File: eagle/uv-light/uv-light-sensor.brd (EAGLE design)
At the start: 17 x 13 mm, 4 parts, among them IC100 SI1147

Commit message: CHG: updated lib, schematics and boards
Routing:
- net GND: vias 0 -> 53
- added copper zone on layer 16, net GND
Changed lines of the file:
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@@
 <element name="IC100" library="weather_station" package="QFN-10/2MM" value="SI1147" x="12.065" y="8.89" smashed="yes" rot="R90">
 <attribute name="DIGIKEY" value="336-2624-1-ND" x="26.035" y="24.13" size="1.778" layer="27" rot="R90" display="off"/>
-<attribute name="NAME" x="14.31625" y="8.89" size="1.016" layer="25" font="vector" ratio="12" rot="R90" align="bottom-center"/>
+<attribute name="NAME" x="11.1125" y="11.45875" size="1.016" layer="25" font="vector" ratio="12" rot="R180" align="center"/>
 </element>
 <element name="C100" library="rcl" package="C0603" value="100n" x="8.255" y="8.5725" smashed="yes">
-<attribute name="NAME" x="7.14375" y="10.00125" size="1.27" layer="25"/>
+<attribute name="NAME" x="8.255" y="10.31875" size="1.016" layer="25" align="center"/>
 <attribute name="VALUE" x="7.62" y="6.6675" size="1.27" layer="27"/>
 </element>
 <element name="LINK" library="pinhead" package="1X06" value="" x="8.255" y="5.23875" smashed="yes">
-<attribute name="NAME" x="11.3538" y="2.30505" size="1.27" layer="25" ratio="10"/>
+<attribute name="NAME" x="8.1788" y="2.7813" size="1.016" layer="25" ratio="10" align="center"/>
 <attribute name="VALUE" x="0.635" y="2.06375" size="1.27" layer="27"/>
 </element>
 <element name="SOLAR" library="pinhead" package="1X02" value="" x="3.175" y="8.5725" smashed="yes" rot="R180">
-<attribute name="NAME" x="6.7437" y="11.5062" size="1.27" layer="25" ratio="10" rot="R180"/>
+<attribute name="NAME" x="3.2512" y="10.8712" size="1.016" layer="25" ratio="10" rot="R180" align="center"/>
 <attribute name="VALUE" x="5.715" y="11.7475" size="1.27" layer="27" rot="R180"/>
 </element>
@@
 <wire x1="11.7475" y1="10.4775" x2="11.815" y2="10.41" width="0.254" layer="1"/>
 <wire x1="11.815" y1="10.41" x2="11.815" y2="9.84" width="0.254" layer="1"/>
-<polygon width="0.4064" layer="1" thermals="no">
+<polygon width="0.3048" layer="1" thermals="no">
 <vertex x="0" y="13"/>
 <vertex x="0" y="0"/>
@@
 <vertex x="17" y="13"/>
 </polygon>
+<via x="3.81" y="0.635" extent="1-16" drill="0.3"/>
+<polygon width="0.3048" layer="16" thermals="no">
+<vertex x="0" y="13"/>
+<vertex x="17" y="13"/>
+<vertex x="17" y="0"/>
+<vertex x="0" y="0"/>
+</polygon>
+<via x="4.7625" y="0.635" extent="1-16" drill="0.3"/>
+<via x="5.715" y="0.635" extent="1-16" drill="0.3"/>
+<via x="6.6675" y="0.635" extent="1-16" drill="0.3"/>
+<via x="7.62" y="0.635" extent="1-16" drill="0.3"/>
+<via x="8.5725" y="0.635" extent="1-16" drill="0.3"/>
+<via x="9.525" y="0.635" extent="1-16" drill="0.3"/>
+<via x="10.4775" y="0.635" extent="1-16" drill="0.3"/>
+<via x="11.43" y="0.635" extent="1-16" drill="0.3"/>
+<via x="12.3825" y="0.635" extent="1-16" drill="0.3"/>
+<via x="13.335" y="0.635" extent="1-16" drill="0.3"/>
+<via x="14.2875" y="0.635" extent="1-16" drill="0.3"/>
+<via x="15.24" y="0.635" extent="1-16" drill="0.3"/>
+<via x="16.1925" y="0.635" extent="1-16" drill="0.3"/>
+<via x="16.35125" y="1.42875" extent="1-16" drill="0.3"/>
+<via x="16.35125" y="2.38125" extent="1-16" drill="0.3"/>
+<via x="16.35125" y="3.33375" extent="1-16" drill="0.3"/>
+<via x="16.35125" y="4.28625" extent="1-16" drill="0.3"/>
+<via x="16.35125" y="5.23875" extent="1-16" drill="0.3"/>
+<via x="16.35125" y="6.19125" extent="1-16" drill="0.3"/>
+<via x="16.35125" y="7.14375" extent="1-16" drill="0.3"/>
+<via x="16.35125" y="8.09625" extent="1-16" drill="0.3"/>
+<via x="16.35125" y="9.04875" extent="1-16" drill="0.3"/>
+<via x="15.39875" y="8.73125" extent="1-16" drill="0.3"/>
+<via x="14.12875" y="9.04875" extent="1-16" drill="0.3"/>
+<via x="12.85875" y="10.95375" extent="1-16" drill="0.3"/>
+<via x="13.17625" y="11.90625" extent="1-16" drill="0.3"/>
+<via x="12.54125" y="12.3825" extent="1-16" drill="0.3"/>
+<via x="11.58875" y="12.3825" extent="1-16" drill="0.3"/>
+<via x="10.63625" y="12.3825" extent="1-16" drill="0.3"/>
+<via x="9.68375" y="12.3825" extent="1-16" drill="0.3"/>
+<via x="8.73125" y="12.3825" extent="1-16" drill="0.3"/>
+<via x="7.77875" y="12.3825" extent="1-16" drill="0.3"/>
+<via x="6.82625" y="12.3825" extent="1-16" drill="0.3"/>
+<via x="5.87375" y="12.3825" extent="1-16" drill="0.3"/>
+<via x="4.92125" y="12.3825" extent="1-16" drill="0.3"/>
+<via x="3.96875" y="12.3825" extent="1-16" drill="0.3"/>
+<via x="3.01625" y="12.3825" extent="1-16" drill="0.3"/>
+<via x="2.06375" y="12.3825" extent="1-16" drill="0.3"/>
+<via x="1.11125" y="12.3825" extent="1-16" drill="0.3"/>
+<via x="0.635" y="11.7475" extent="1-16" drill="0.3"/>
+<via x="0.635" y="10.795" extent="1-16" drill="0.3"/>
+<via x="0.635" y="9.8425" extent="1-16" drill="0.3"/>
+<via x="0.635" y="8.89" extent="1-16" drill="0.3"/>
+<via x="0.635" y="7.9375" extent="1-16" drill="0.3"/>
+<via x="0.635" y="6.985" extent="1-16" drill="0.3"/>
+<via x="0.635" y="6.0325" extent="1-16" drill="0.3"/>
+<via x="0.635" y="5.08" extent="1-16" drill="0.3"/>
+<via x="0.635" y="3.81" extent="1-16" drill="0.3"/>
+<via x="3.175" y="3.81" extent="1-16" drill="0.3"/>
+<via x="3.81" y="3.175" extent="1-16" drill="0.3"/>
+<via x="4.1275" y="2.2225" extent="1-16" drill="0.3"/>
+<via x="4.1275" y="1.42875" extent="1-16" drill="0.3"/>
 </signal>
 <signal name="N$1">

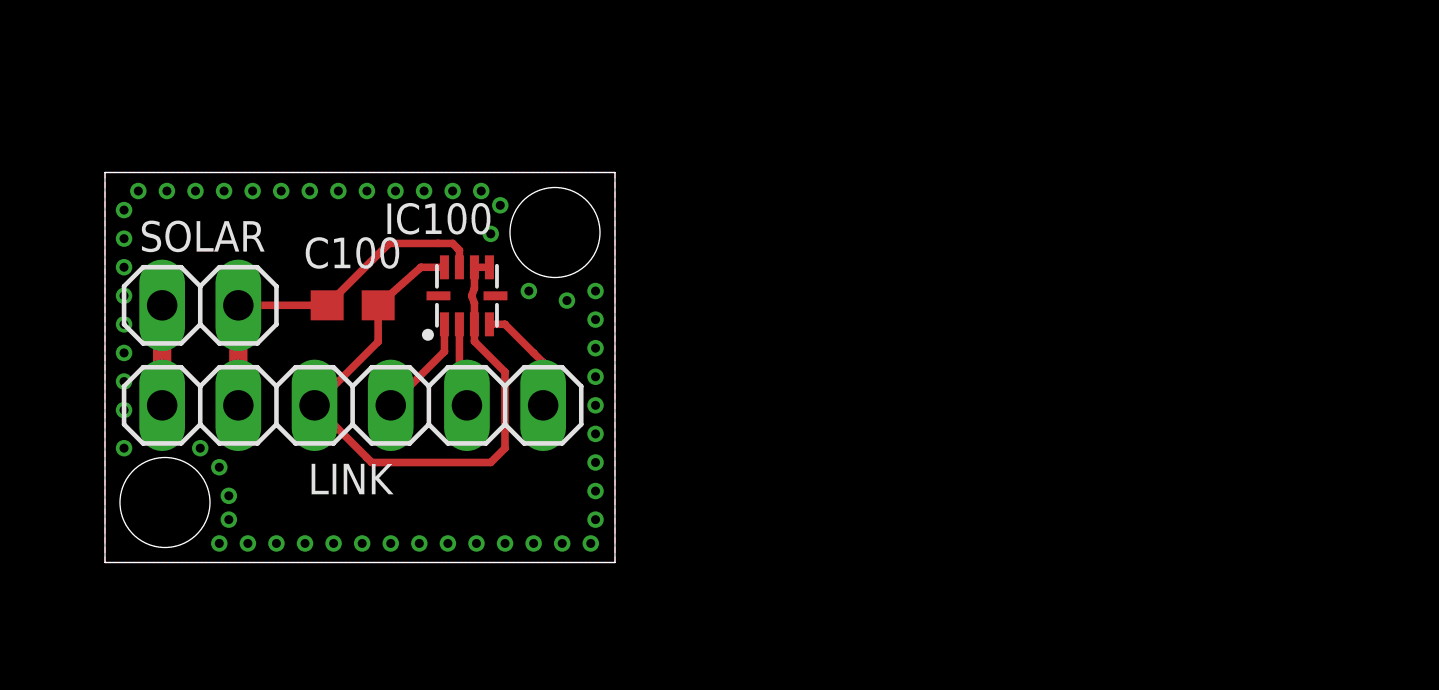
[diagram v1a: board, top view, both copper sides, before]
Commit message: CHG: Replaced Si1147 through Si1133
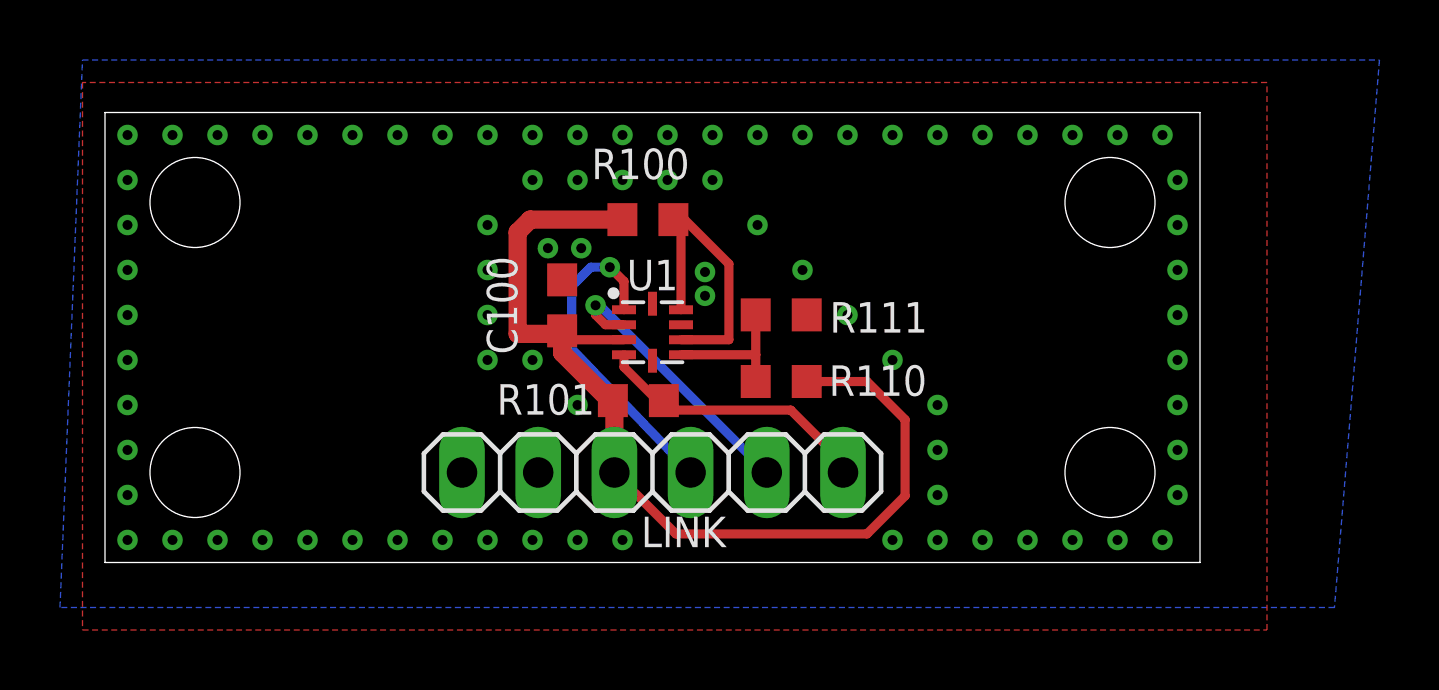
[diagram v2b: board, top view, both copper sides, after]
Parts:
- removed IC100: SI1147, weather_station:QFN-10/2MM
- removed SOLAR: (no value), pinhead:1X02
- added R100: 10k, rcl:R0603
- added R101: 4k7, rcl:R0603
- added R110: 47k, rcl:R0603
- added R111: DNB, rcl:R0603
- added U1: SI1133AA00-GMR, weather_station:QFN-10/2MM
- moved LINK 10.2 mm to (18.2, 3.00)
- moved C100 6.98 mm to (15.2, 8.57), turned to 270 degrees
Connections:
- removed net N$4: LINK.1, SOLAR.2
- new net N$5: R100.1, U1.7, U1.9
- new net N$6: R110.1, R111.1, U1.6
- net GND: now also R111.2, U1.8; no longer IC100.8, SOLAR.1
- net N$1: now also R101.1, U1.4; no longer IC100.4
- net N$2: now also U1.2; no longer IC100.2
- net N$3: now also U1.1; no longer IC100.1
- net VCC: now also R100.2, R101.2, R110.2, U1.3; no longer IC100.3, IC100.6, IC100.7, IC100.9
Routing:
- net VCC: track 21.2 -> 33.7 mm
- net GND: track 12.2 -> 0.00 mm, vias 53 -> 81
- net N$5: track 0.00 -> 9.69 mm
- net N$3: track 3.44 -> 10.9 mm, vias 0 -> 1
- net N$2: track 2.80 -> 9.42 mm, vias 0 -> 1
- net N$1: track 3.75 -> 9.37 mm
- net N$6: track 0.00 -> 4.72 mm
- net N$4: track 3.33 -> 0.00 mm
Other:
- board size 17 x 13 mm -> 36.5 x 15 mm
